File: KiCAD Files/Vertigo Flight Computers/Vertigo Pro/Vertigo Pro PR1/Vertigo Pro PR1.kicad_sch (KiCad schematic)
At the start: 145 parts, among them IC1 ICM-20602, IC2 DPS310XTSA1, IC3 MLX90393SLW-ABA-011-RE, J1 ST-LINK Conn, J2 USB_C_Receptacle_USB2.0, J3 FFC2A32-24-T, J4 Screw_Terminal, J5 Screw_Terminal, J6 Screw_Terminal, J7 Screw_Terminal, Q1 IRF530SPBF, Q2 IRF530SPBF, Q3 IRF530SPBF, Q4 IRF530SPBF, Q5 SI7149ADP-T1-GE3, SW1 SW_SPDT, U1 STM32F103C8Tx, U10 TPS79133DBVR, U11 TLV709, U12 TLV709, U13 TLV75528PDBV, U2 AP63203WU, U3 ESP32-S3-WROOM-1, U4 TLV75515PDBV, U6 W25Q64FV, U7 TPS2121RUXR, U8 NEO-6M-GPS, U9 24AA32A-I_MS, Y1 16MHz

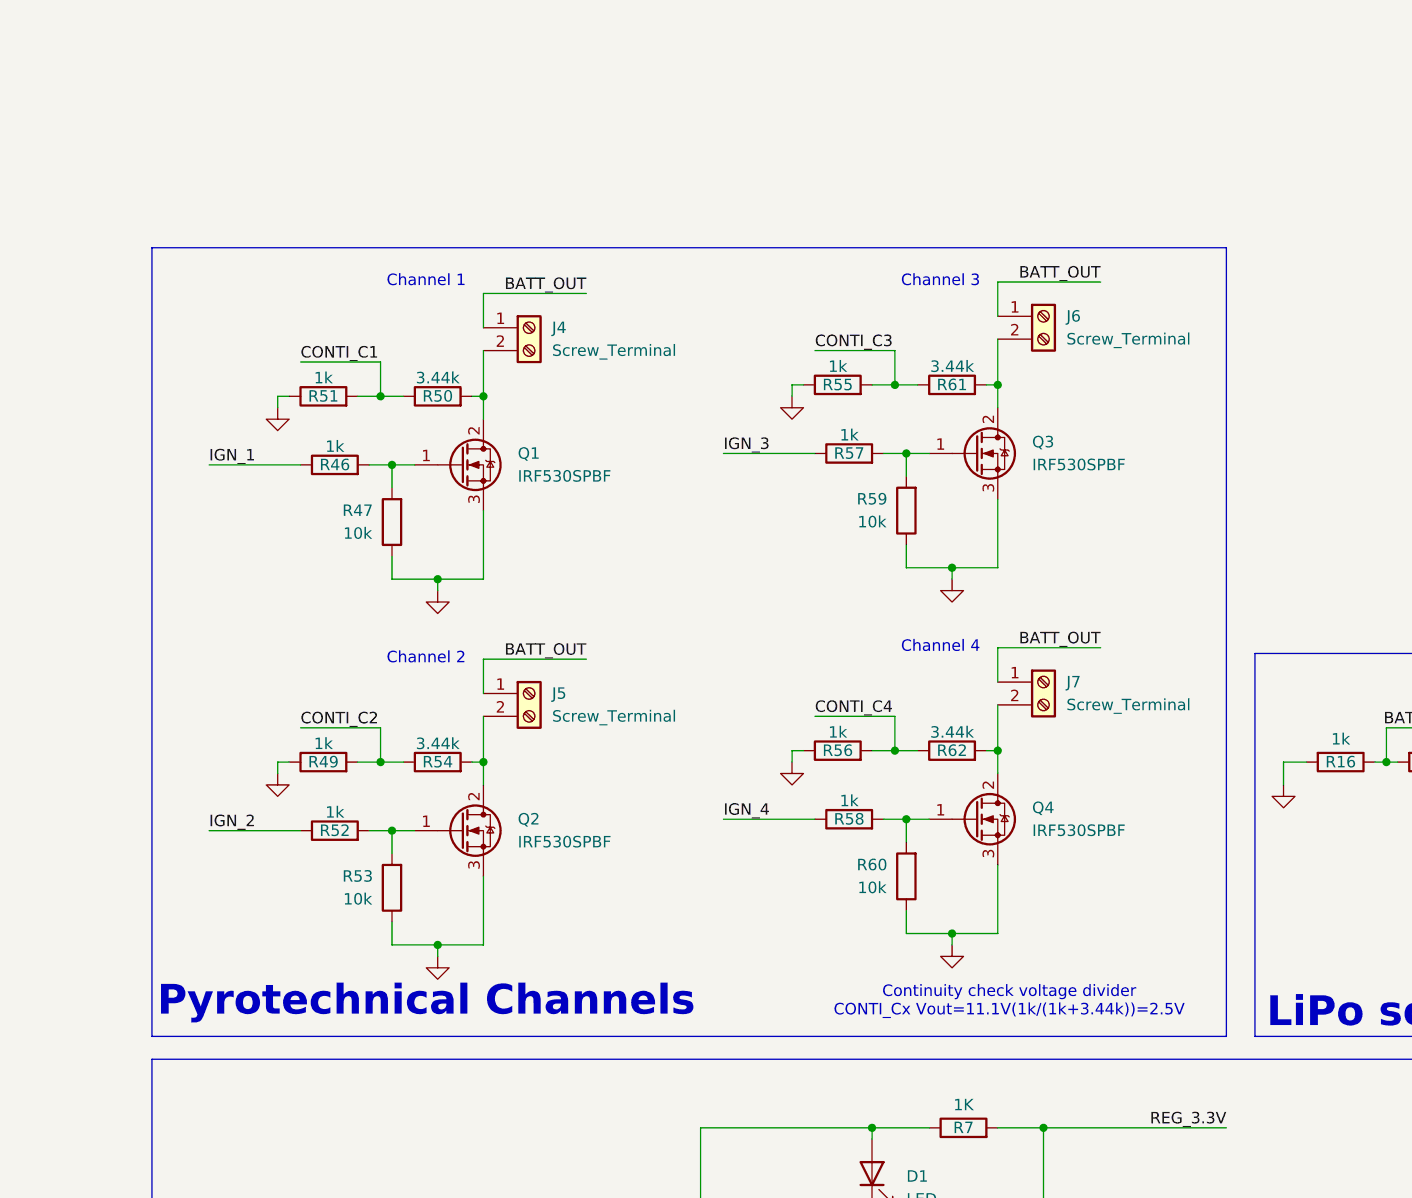
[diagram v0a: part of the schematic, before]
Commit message: New pyro circuitry
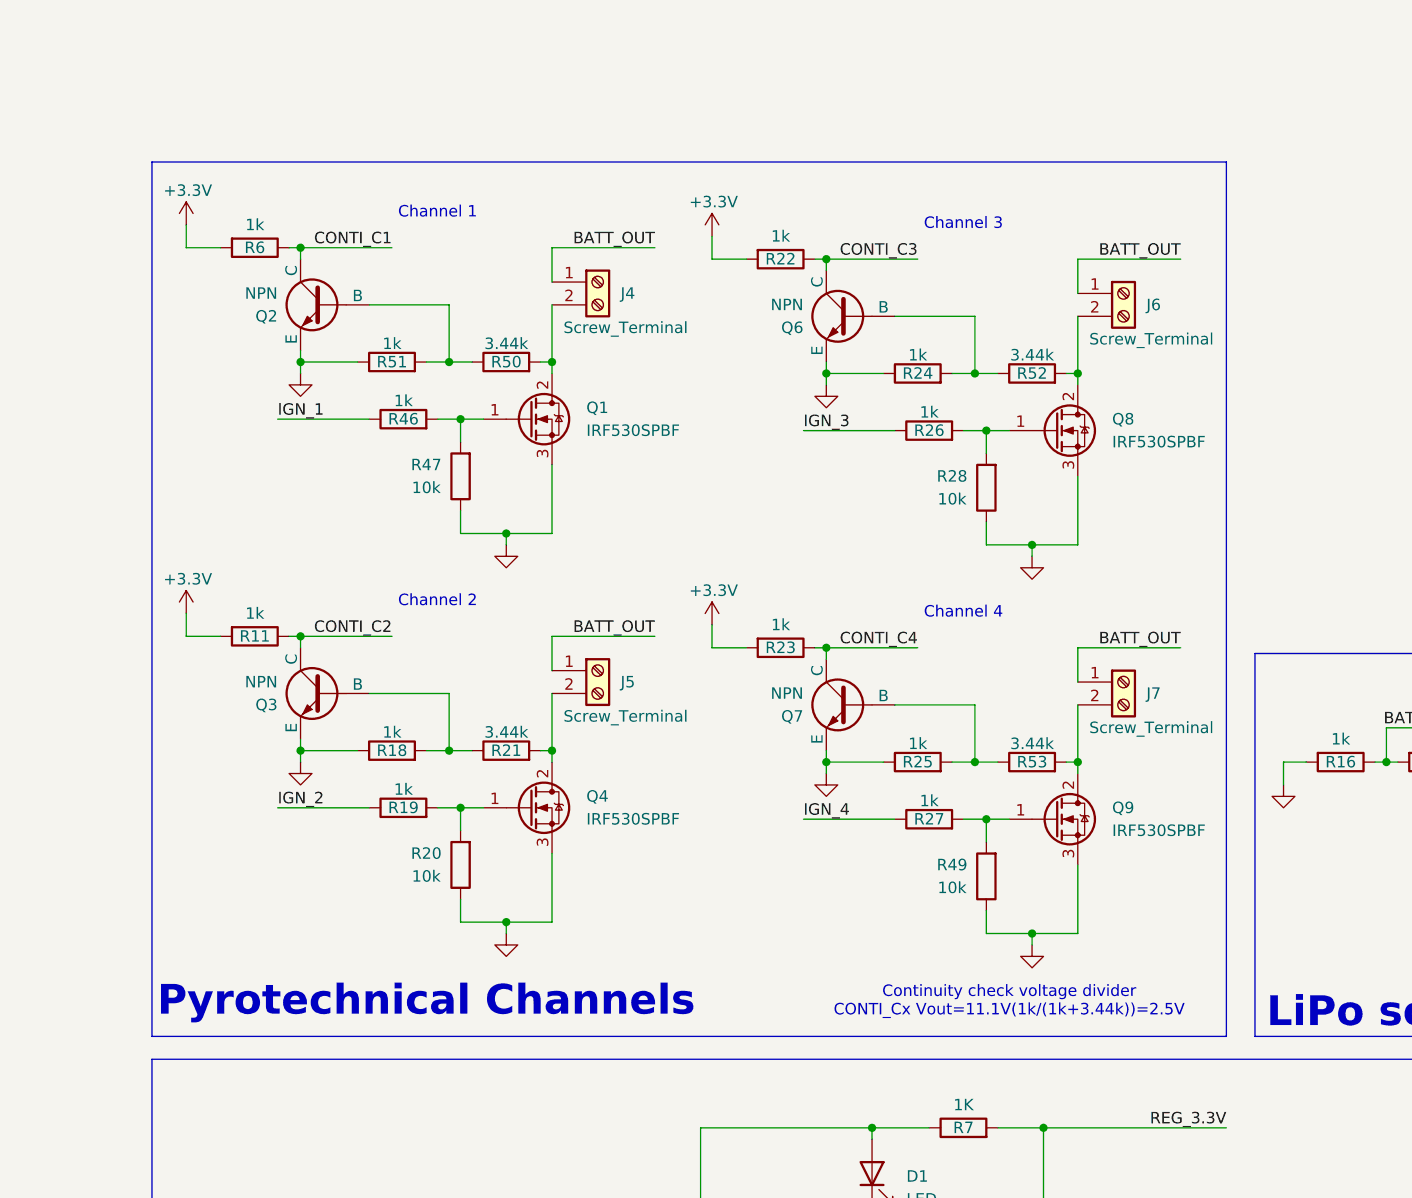
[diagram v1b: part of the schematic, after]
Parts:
- removed Q2, Q3: IRF530SPBF, Package_TO_SOT_SMD:TO-263-2, symbol Device:Q_NMOS_GDS
- removed R54, R61, R62: 3.44k, Resistor_SMD:R_0603_1608Metric, symbol Device:R
- removed R55, R56, R57, R58: 1k, Resistor_SMD:R_0603_1608Metric, symbol Device:R
- removed R59, R60: 10k, Resistor_SMD:R_0603_1608Metric, symbol Device:R
- added Q2, Q3, Q6, Q7: NPN, symbol Simulation_SPICE:NPN
- added Q8, Q9: IRF530SPBF, Package_TO_SOT_SMD:TO-263-2, symbol Device:Q_NMOS_GDS
- added R11, R18, R19, R22, R23, R24, R25, R26, R27, R6: 1k, Resistor_SMD:R_0603_1608Metric, symbol Device:R
- added R20, R28: 10k, Resistor_SMD:R_0603_1608Metric, symbol Device:R
- added R21: 3.44k, Resistor_SMD:R_0603_1608Metric, symbol Device:R
- R49: value 1k -> 10k
- R52: value 1k -> 3.44k
- R53: value 10k -> 3.44k
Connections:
- net +3.3V: now also R11.2, R22.2, R23.2, R6.2
- net AGND: now also Q2.3 (E), Q3.3 (E), Q6.3 (E), Q7.3 (E), Q8.3 (S), Q9.3 (S), R18.1, R20.1, R24.1, R25.1, R28.1; no longer R53.1
- net CONTI_C1: now also Q2.1 (C), R6.1; no longer R50.1, R51.2
- net CONTI_C2: now also Q3.1 (C), R11.1; no longer R49.2
- net CONTI_C3: now also Q6.1 (C), R22.1
- net CONTI_C4: now also Q7.1 (C), R23.1
- net IGN_2: now also R19.1; no longer R52.1
- net IGN_3: now also R26.1
- net IGN_4: now also R27.1
- net at J6.2 (Pin_2): now also R52.2, Q8.2 (D)
- net at Q4.2 (D): now also J5.2 (Pin_2), R21.2; no longer J7.2 (Pin_2)
- net at R53.2: now also J7.2 (Pin_2), Q9.2 (D); no longer R52.2
- net at Q4.1 (G): now also R19.2, R20.2
- new net: Q8.1 (G), R26.2, R28.2
- new net: Q7.2 (B), R25.2, R53.1
- new net: Q6.2 (B), R24.2, R52.1
- new net: Q2.2 (B), R50.1, R51.2
- new net: Q9.1 (G), R27.2, R49.2
- new net: Q3.2 (B), R18.2, R21.1
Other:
- moved on the sheet: J4, Q1, R46, R47, R50, R51

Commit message: Flash fix
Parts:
- removed R31, R32, R33: 10K, Resistor_SMD:R_0603_1608Metric, symbol Device:R
- R16: value 1k -> 20k
- R17: value 3k -> 60k
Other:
- moved on the sheet: U6

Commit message: fix
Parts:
- removed C37: 2.2uF, Capacitor_SMD:C_0402_1005Metric_Pad0.74x0.62mm_HandSolder, symbol Device:C
- removed C38: 2.2uF, Capacitor_SMD:C_0603_1608Metric_Pad1.08x0.95mm_HandSolder, symbol Device:C
- removed IC3: MLX90393SLW-ABA-011-RE, symbol SamacSys_Parts:MLX90393SLW-ABA-011-RE
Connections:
- no-connect marks 32 -> 24
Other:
- note removed: "Primary Magnetometer"
- note removed: "Provide adequate separation distance to devices that contain permanent magnets or generate magnetic fields (e.g. speakers, coils, inductors), or main power traces etc."
- moved on the sheet: C31, C32, C33, C34, C35, C36, IC1, IC2, R29, R30

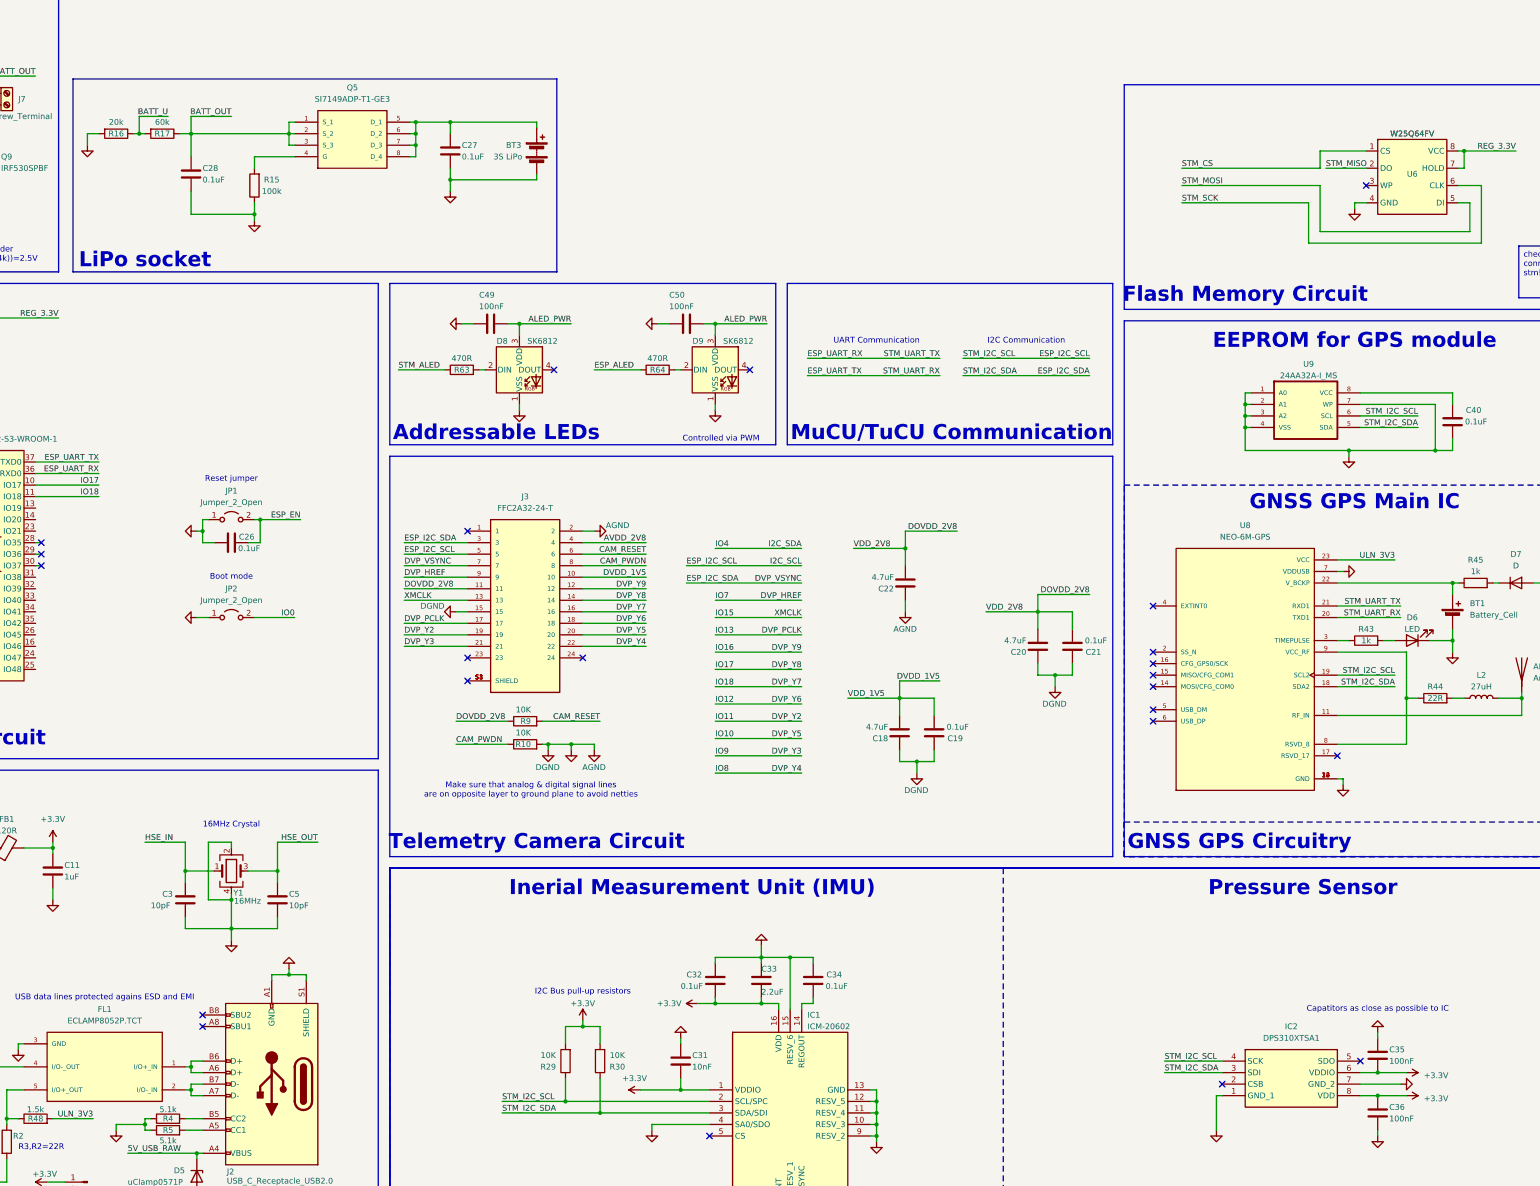
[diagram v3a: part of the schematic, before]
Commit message: ULN Reg to sensors
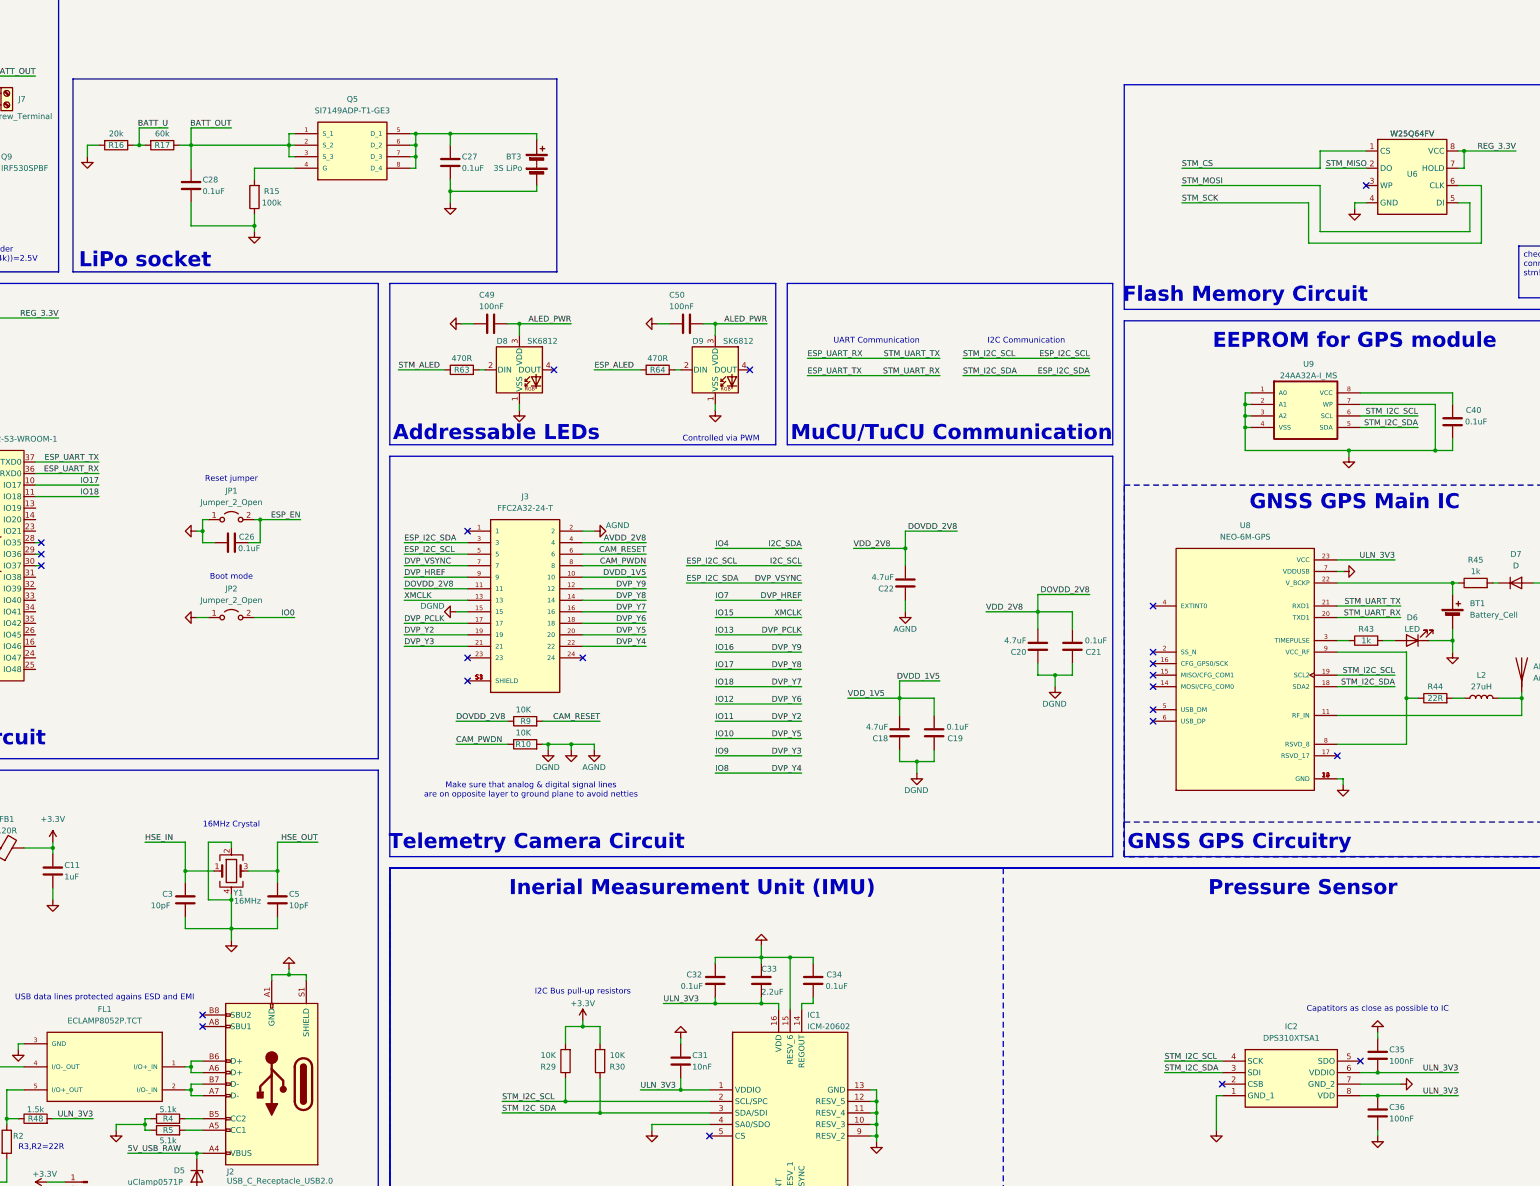
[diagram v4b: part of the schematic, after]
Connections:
- net +3.3V: no longer C31.2, C32.2, C33.2, C35.2, C36.1, IC1.1 (VDDIO), IC1.16 (VDD), IC2.6 (VDDIO), IC2.8 (VDD)
- net ULN_3V3: now also C31.2, C32.2, C33.2, C35.2, C36.1, IC1.1 (VDDIO), IC1.16 (VDD), IC2.6 (VDDIO), IC2.8 (VDD)
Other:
- moved on the sheet: BT3, C27, C28, Q5, R15, R16, R17

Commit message: Fix
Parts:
- removed BT1: Battery_Cell, symbol Device:Battery_Cell
- Q2, Q3, Q6, Q7: value NPN -> MMBT3904-TP; footprint (none) -> Package_TO_SOT_SMD:SOT-23_Handsoldering
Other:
- moved on the sheet: C20, C21, C26, JP1, JP2

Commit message: Power LEDs for uCs + fix
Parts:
- added D2: MuCU LED, Resistor_SMD:R_0603_1608Metric, symbol Device:LED
- added R31: 1K, Resistor_SMD:R_0603_1608Metric, symbol Device:R
- D1: value LED -> TuCU LED
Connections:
- net +3.3V: now also R31.1
- net AGND: now also D2.1 (K)
- net CONTI_C2: now also U1.15 (PA5)
- net CONTI_C3: now also U1.16 (PA6)
- net CONTI_C4: now also U1.17 (PA7)
- new net: D2.2 (A), R31.2
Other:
- note added: "High G-force Inerial Measurement Unit"
- note added: "Low G-force Inerial Measurement Unit (IMU)"
- note added: "Primary Pressure Sensor"
- note removed: "Inerial Measurement Unit (IMU)"
- note removed: "Pressure Sensor"
- moved on the sheet: C16, C17, C25, C26, C31, C32, C33, C34, C35, C36, D1, IC1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

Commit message: Fix
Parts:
- L2: footprint (none) -> Inductor_SMD:L_0805_2012Metric_Pad1.15x1.40mm_HandSolder
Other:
- moved on the sheet: AE1, BT3, C18, C19, C20, C21, C22, C27, C28, C31, C32, C33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

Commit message: Pyro fix, est
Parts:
- R11, R22, R23, R6: value 1k -> 10k
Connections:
- net +3.3V: now also C31.2, C35.2, IC1.1 (VDDIO), IC2.6 (VDDIO), U8.23 (VCC)
- net ULN_3V3: no longer C31.2, C35.2, IC1.1 (VDDIO), IC2.6 (VDDIO), U8.23 (VCC)
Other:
- moved on the sheet: BT3, C31, C32, C33, C34, IC1, R29, R30
